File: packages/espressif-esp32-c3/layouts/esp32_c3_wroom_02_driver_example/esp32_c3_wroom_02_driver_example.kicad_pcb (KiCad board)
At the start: 2 copper layers, 12 parts

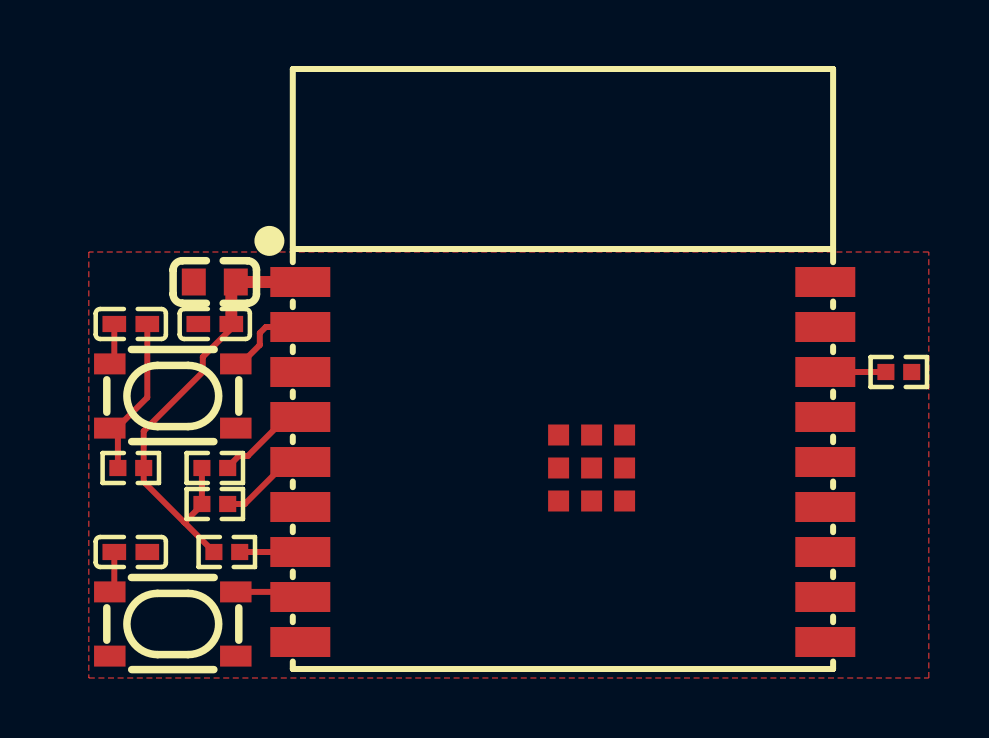
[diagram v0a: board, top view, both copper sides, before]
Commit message: connect I2C, SPI, and I2S to some sensible default gpio
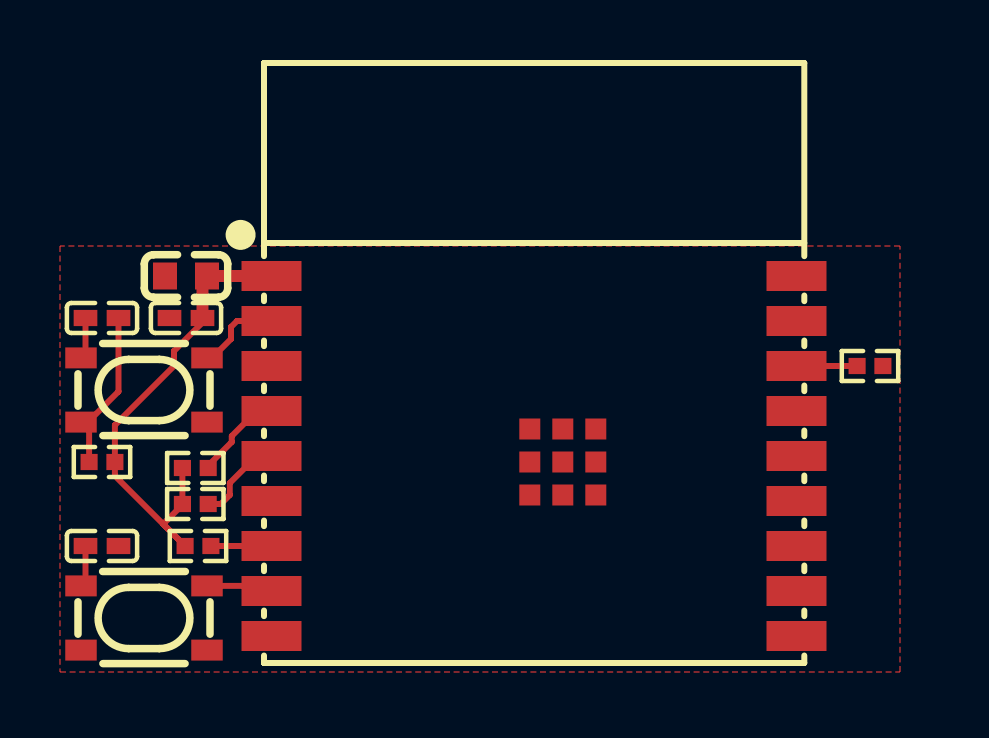
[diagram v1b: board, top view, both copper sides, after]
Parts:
- moved C3 0.98 mm to (-12.6, -6.20)
- moved C4 0.98 mm to (-12.6, -4.80)
- moved R2 0.98 mm to (-12.2, 2.80)
- moved SW1 0.98 mm to (-14.0, 5.20)
- moved SW2 0.98 mm to (-14.0, -2.40)
- moved U1 0.98 mm to (-0.96, -0.20)
- moved C1 0.98 mm to (-15.4, 2.80)
- moved C2 0.98 mm to (-15.4, -4.80)
- moved R1 0.98 mm to (10.2, -3.20)
- moved R3 0.98 mm to (-15.4, 0.00)
- moved R4 0.65 mm to (-12.2, 0.20)
- moved R5 0.65 mm to (-12.2, 1.40)
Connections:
- net mcu-line renamed mcu_module-line
- net mcu.esp32_module-line-0 renamed mcu_module.esp32_c3-line-0
- net mcu.esp32_module-line-1 renamed mcu_module.esp32_c3-line-1
- net mcu.esp32_module-line-2 renamed mcu_module.esp32_c3-line-2
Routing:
- net hv: track 15.4 -> 16.6 mm

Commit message: fix enable pin pullup
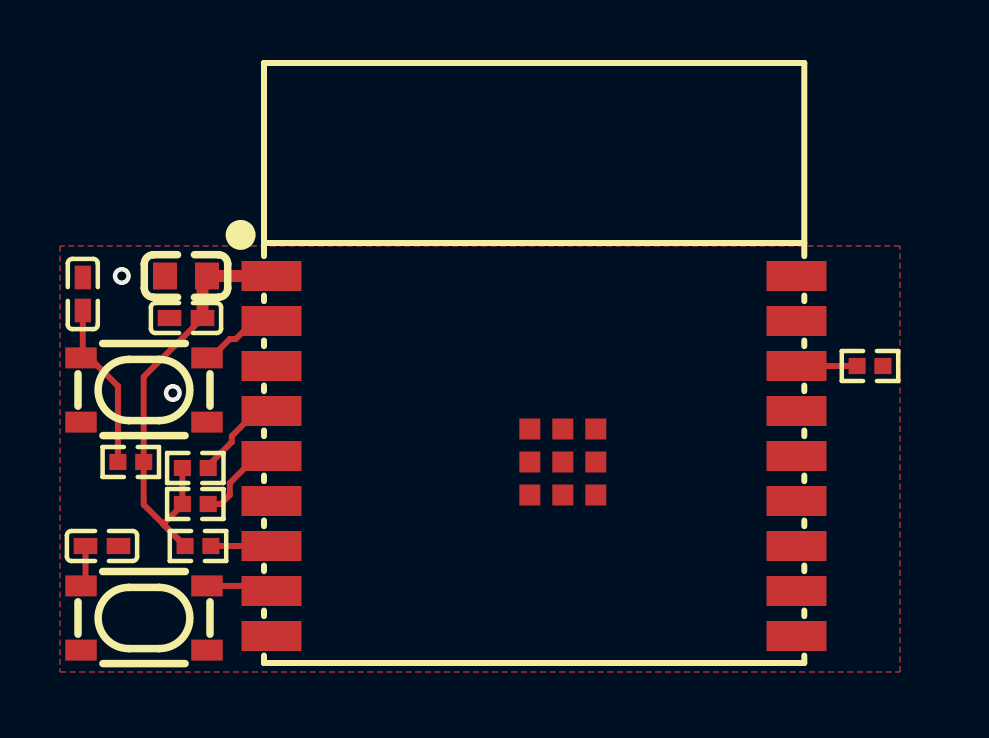
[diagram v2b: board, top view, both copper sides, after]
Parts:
- moved C2 1.02 mm to (-16.0, -5.60), turned to -90 degrees
- moved R3 0.96 mm to (-14.4, 0.00), turned to 180 degrees
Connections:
- C2 pad 1: input -> gnd
- R3 pad 1: input -> hv
- R3 pad 2: hv -> output-1
- SW2 pad 1: input -> gnd
- SW2 pad 2: input -> gnd
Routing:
- net input: track 5.56 -> 0.00 mm
- net output-1: track 4.29 -> 8.41 mm
- net hv: track 16.6 -> 15.8 mm
- net gnd: vias 0 -> 2

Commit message: expose ifs in driver, clean-up legacy folders
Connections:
- net RXD renamed mcu_module-line-4
- net TXD renamed mcu_module-line-5
- net mcu_module-line renamed mcu_module-line-0
- net mcu_module.esp32_c3-line-0 renamed mcu_module-line-1
- net mcu_module.esp32_c3-line-1 renamed mcu_module-line-2
- net mcu_module.esp32_c3-line-2 renamed mcu_module-line-3
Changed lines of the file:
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@@
     (net 1 "-line-7")
     (net 2 "-line-3")
-    (net 3 "mcu_module.esp32_c3-line-2")
+    (net 3 "mcu_module-line-3")
     (net 4 "-line-4")
-    (net 5 "RXD")
+    (net 5 "mcu_module-line-4")
     (net 6 "-line-6")
     (net 7 "-line-5")
-    (net 8 "TXD")
+    (net 8 "mcu_module-line-5")
     (net 9 "-line-2")
     (net 10 "-line-0")
-    (net 11 "mcu_module.esp32_c3-line-0")
-    (net 12 "mcu_module.esp32_c3-line-1")
+    (net 11 "mcu_module-line-1")
+    (net 12 "mcu_module-line-2")
     (net 13 "output-0")
-    (net 14 "mcu_module-line")
+    (net 14 "mcu_module-line-0")
     (net 15 "-line-1")
     (net 16 "hv")
@@
             (size 2 1)
             (layers "F.Cu" "F.Mask" "F.Paste")
-            (net 12 "mcu_module.esp32_c3-line-1")
+            (net 12 "mcu_module-line-2")
         )
         (pad "4" smd rect
@@
             (size 2 1)
             (layers "F.Cu" "F.Mask" "F.Paste")
-            (net 5 "RXD")
+            (net 5 "mcu_module-line-4")
         )
         (pad "12" smd rect
@@
             (size 2 1)
             (layers "F.Cu" "F.Mask" "F.Paste")
-            (net 8 "TXD")
+            (net 8 "mcu_module-line-5")
         )
         (pad "13" smd rect
@@
             (size 2 1)
             (layers "F.Cu" "F.Mask" "F.Paste")
-            (net 3 "mcu_module.esp32_c3-line-2")
+            (net 3 "mcu_module-line-3")
         )
         (pad "15" smd rect
@@
             (size 2 1)
             (layers "F.Cu" "F.Mask" "F.Paste")
-            (net 11 "mcu_module.esp32_c3-line-0")
+            (net 11 "mcu_module-line-1")
         )
         (pad "16" smd rect
@@
             (size 2 1)
             (layers "F.Cu" "F.Mask" "F.Paste")
-            (net 14 "mcu_module-line")
+            (net 14 "mcu_module-line-0")
         )
         (pad "17" smd rect
@@
             (size 0.57 0.54)
             (layers "F.Cu" "F.Mask" "F.Paste")
-            (net 14 "mcu_module-line")
+            (net 14 "mcu_module-line-0")
         )
         (pad "2" smd rect

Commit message: fix dual use of gpio 18
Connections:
- U1 pad 13: -line-4 -> mcu_module-line-2
- U1 pad 15: mcu_module-line-1 -> -line-4
- U1 pad 3: mcu_module-line-2 -> mcu_module-line-1
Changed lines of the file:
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@@
     (net 2 "-line-3")
     (net 3 "mcu_module-line-3")
-    (net 4 "-line-4")
+    (net 4 "mcu_module-line-2")
     (net 5 "mcu_module-line-4")
     (net 6 "-line-6")
@@
     (net 9 "-line-2")
     (net 10 "-line-0")
-    (net 11 "mcu_module-line-1")
-    (net 12 "mcu_module-line-2")
+    (net 11 "-line-4")
+    (net 12 "mcu_module-line-1")
     (net 13 "output-0")
     (net 14 "mcu_module-line-0")
@@
             (size 2 1)
             (layers "F.Cu" "F.Mask" "F.Paste")
-            (net 12 "mcu_module-line-2")
+            (net 12 "mcu_module-line-1")
         )
         (pad "4" smd rect
@@
             (size 2 1)
             (layers "F.Cu" "F.Mask" "F.Paste")
-            (net 4 "-line-4")
+            (net 4 "mcu_module-line-2")
         )
         (pad "14" smd rect
@@
             (size 2 1)
             (layers "F.Cu" "F.Mask" "F.Paste")
-            (net 11 "mcu_module-line-1")
+            (net 11 "-line-4")
         )
         (pad "16" smd rect
